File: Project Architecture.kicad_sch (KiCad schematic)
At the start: 0 parts

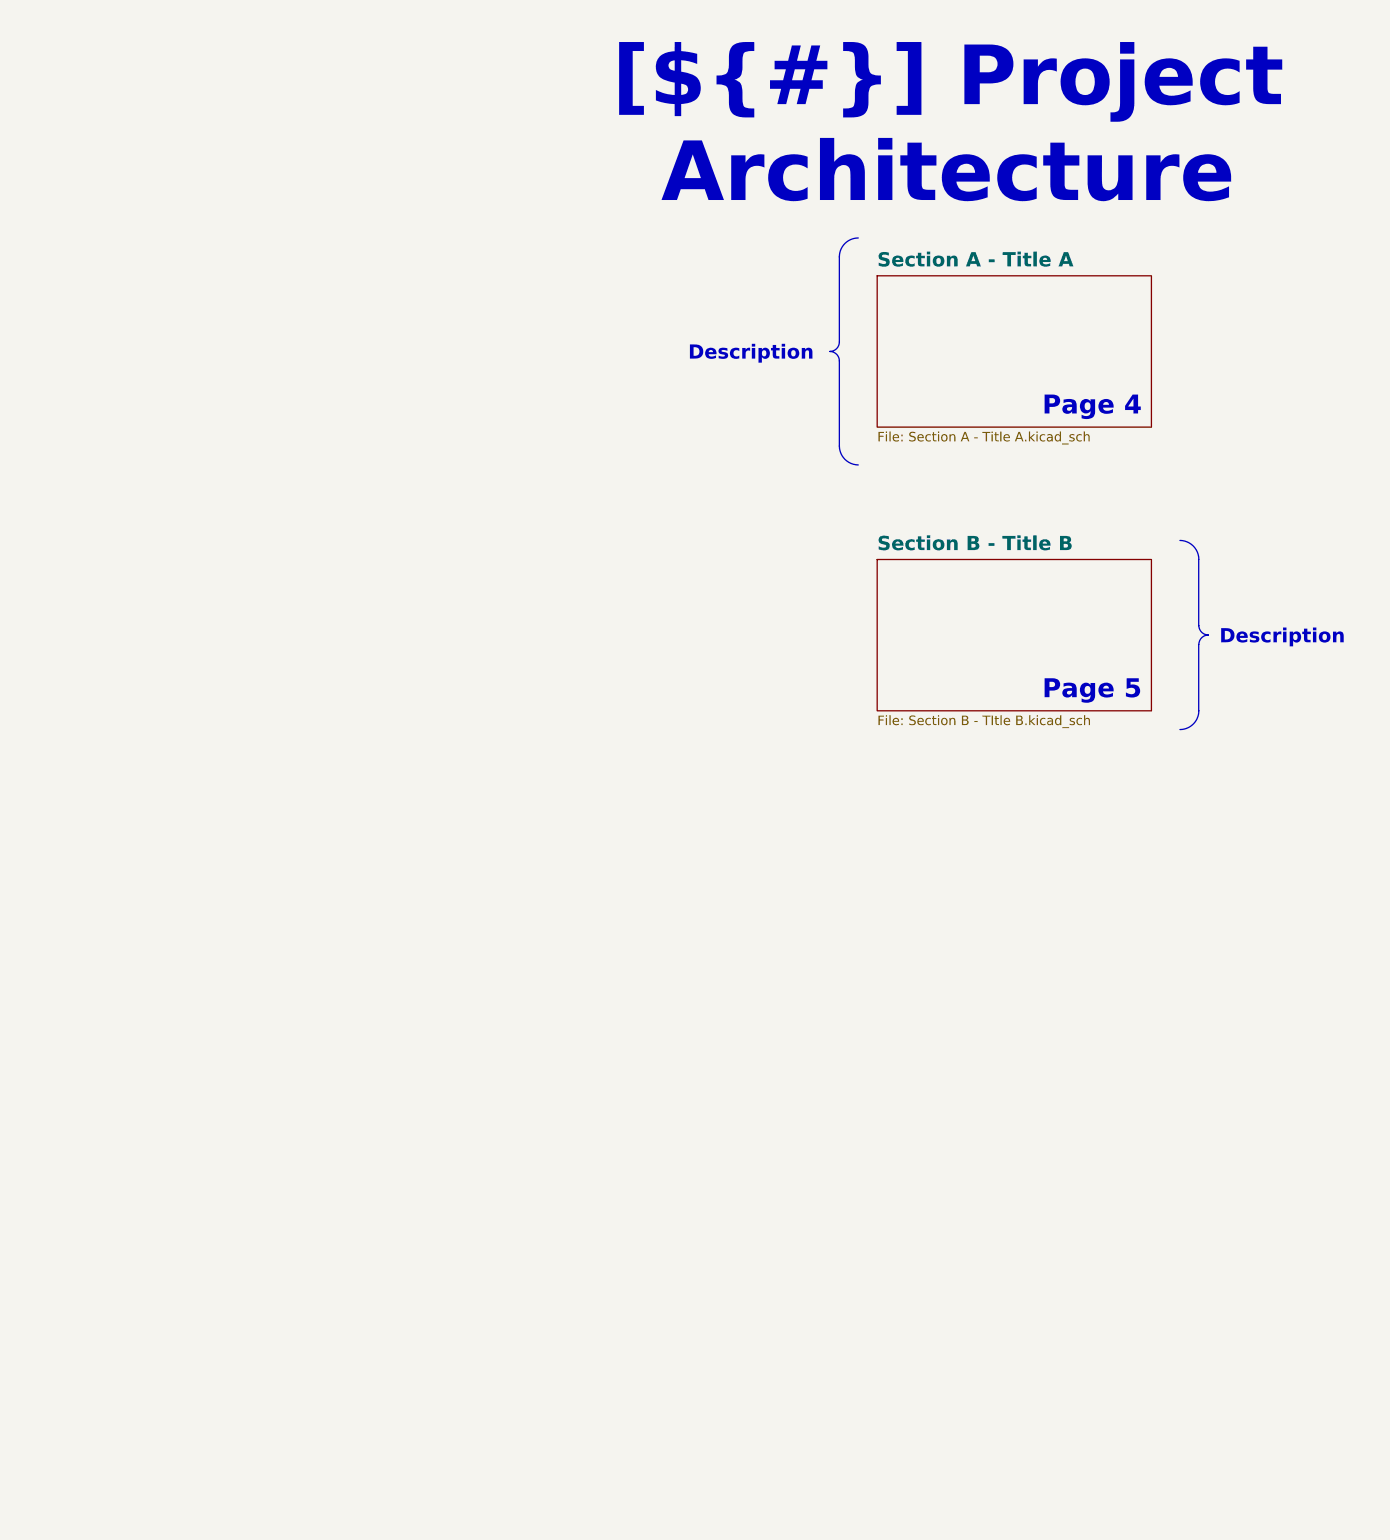
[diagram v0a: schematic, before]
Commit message: chore: Update project file names and paths for Linux-Kit
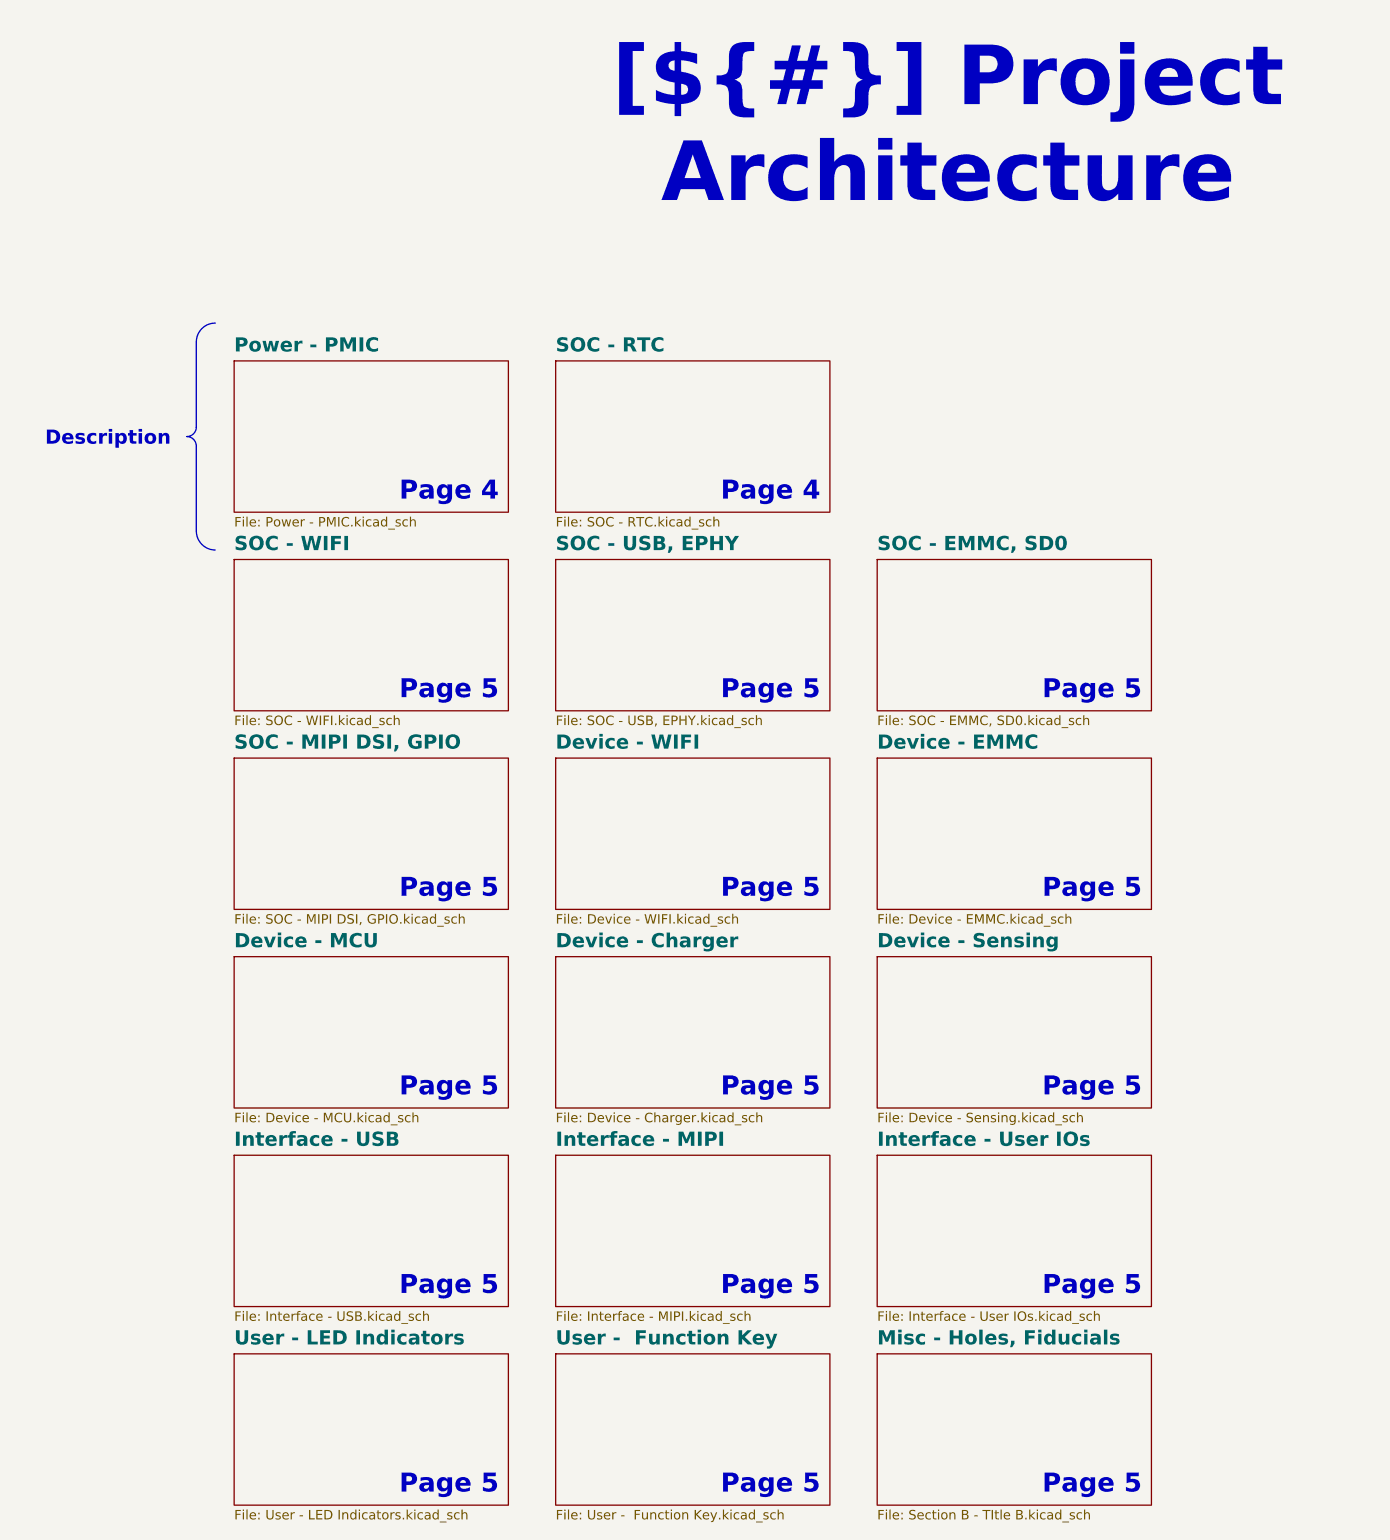
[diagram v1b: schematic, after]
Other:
- sheet Section A - Title A renamed Power - PMIC
- sheet Section B - Title B renamed SOC - EMMC, SD0
- added sheet Device - Charger (Device - Charger.kicad_sch)
- added sheet Device - EMMC (Device - EMMC.kicad_sch)
- added sheet Device - MCU (Device - MCU.kicad_sch)
- added sheet Device - Sensing (Device - Sensing.kicad_sch)
- added sheet Device - WIFI (Device - WIFI.kicad_sch)
- added sheet Interface - MIPI (Interface - MIPI.kicad_sch)
- added sheet Interface - USB (Interface - USB.kicad_sch)
- added sheet Interface - User IOs (Interface - User IOs.kicad_sch)
- added sheet Misc - Holes, Fiducials (Section B - TItle B.kicad_sch)
- added sheet SOC - MIPI DSI, GPIO (SOC - MIPI DSI, GPIO.kicad_sch)
- added sheet SOC - RTC (SOC - RTC.kicad_sch)
- added sheet SOC - USB, EPHY (SOC - USB, EPHY.kicad_sch)
- added sheet SOC - WIFI (SOC - WIFI.kicad_sch)
- added sheet User -  Function Key (User -  Function Key.kicad_sch)
- added sheet User - LED Indicators (User - LED Indicators.kicad_sch)
- sheet Power - PMIC: file Section A - Title A.kicad_sch -> Power - PMIC.kicad_sch
- sheet SOC - EMMC, SD0: file Section B - TItle B.kicad_sch -> SOC - EMMC, SD0.kicad_sch

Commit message: daily updates
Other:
- sheet SOC - RTC renamed SOC - Main
- removed sheet SOC - EMMC, SD0
- removed sheet SOC - MIPI DSI, GPIO
- removed sheet SOC - USB, EPHY
- removed sheet SOC - WIFI
- sheet SOC - Main: file SOC - RTC.kicad_sch -> SOC - Main.kicad_sch
